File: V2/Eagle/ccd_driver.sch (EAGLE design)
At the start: 103 parts, among them J3 POWER_JACK, Q1 1A/60V/2.4Ω, Q2 BC214, Q3 2N2222, U1 LM358DT, U10 TPD4S012DRYR, U11 0ZCJ0050FF2G, U12 REF3025AIDBZR, U2 MK02FN128VLF10, U5 CP2102N-A01-GQFN20R

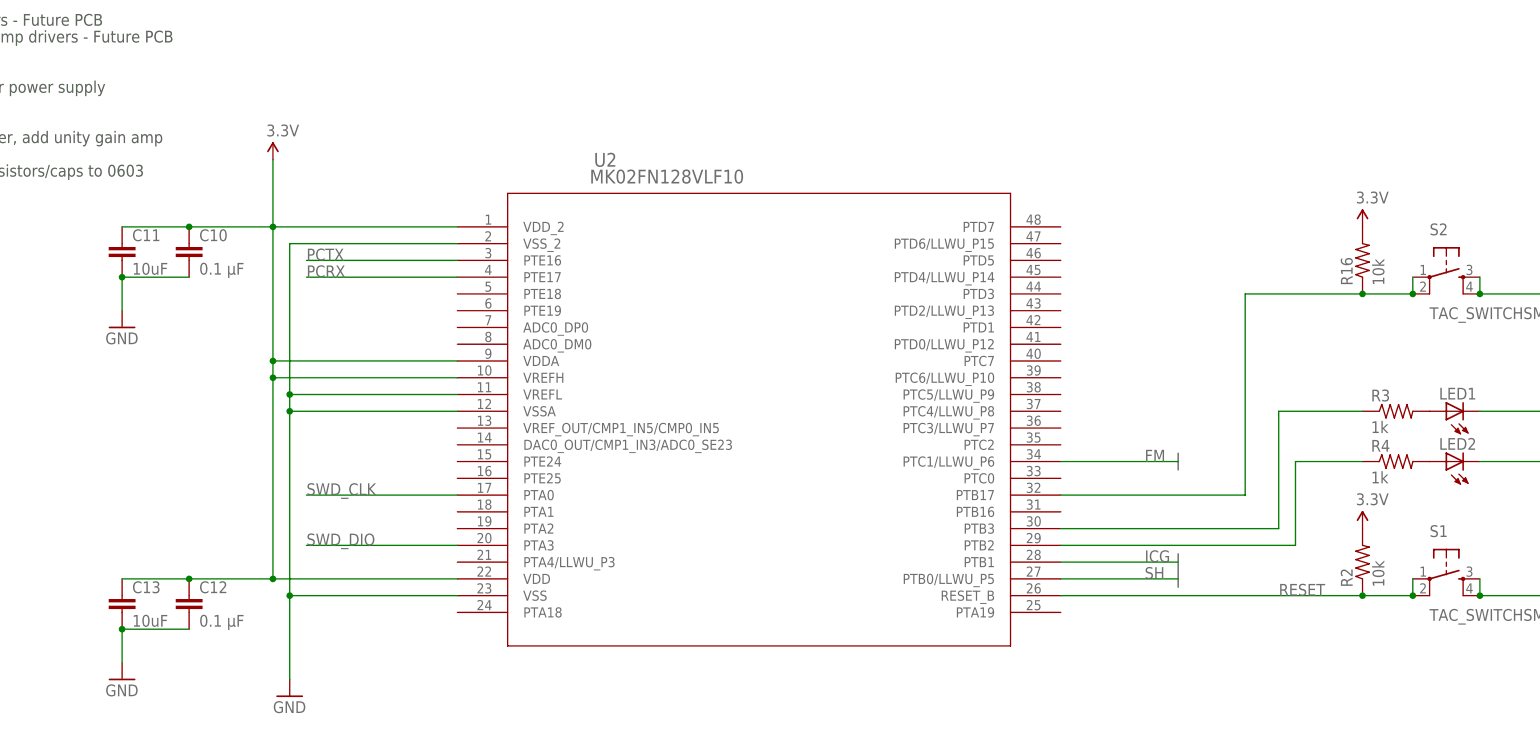
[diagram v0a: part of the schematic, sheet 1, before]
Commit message: changed most caps and resistors to 0603
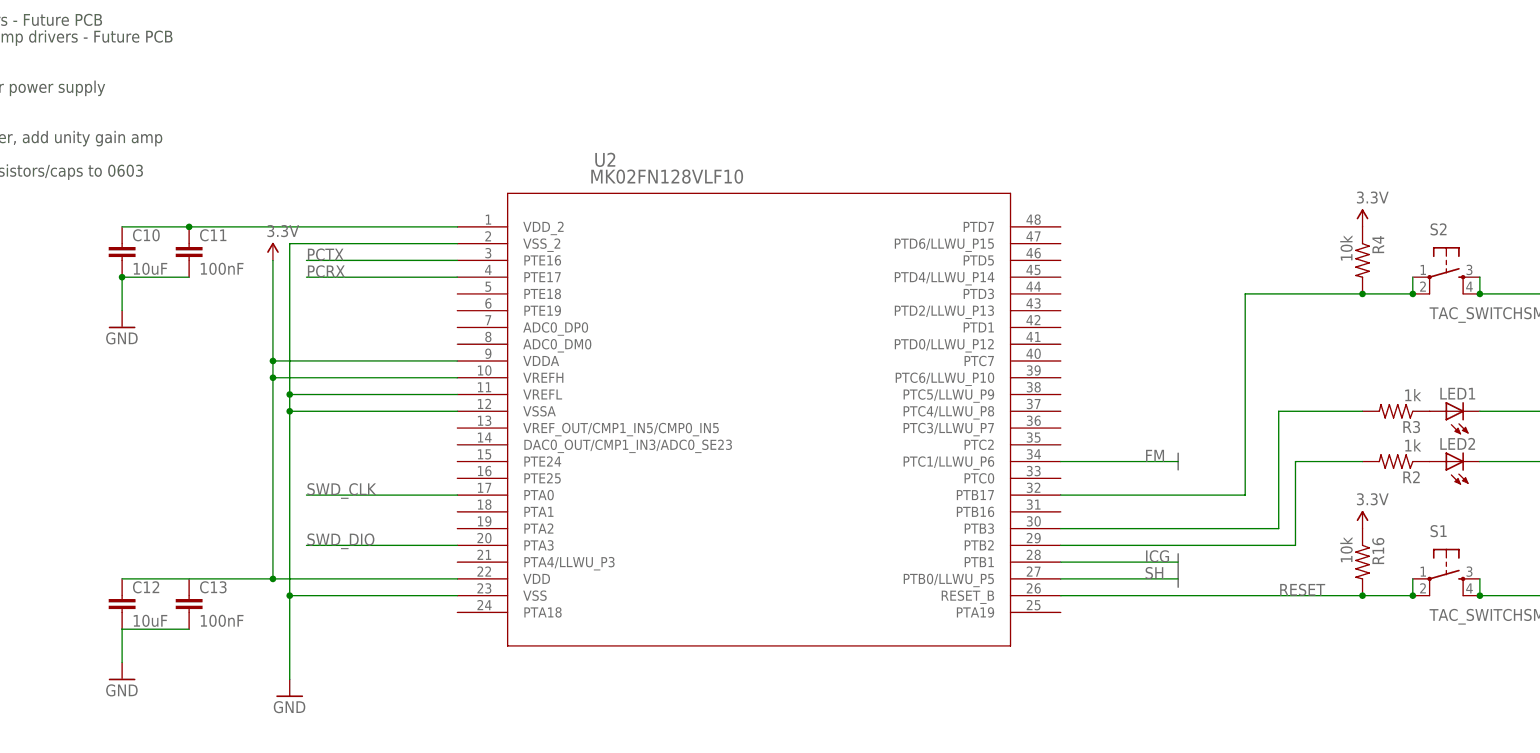
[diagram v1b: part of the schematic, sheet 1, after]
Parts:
- C10, C12: value 0.1 µF -> 10uF; device resistor:C-EUC1206 -> SparkFun-Capacitors:0.1UF-0603-25V-(+80/-20%)
- C11, C13: value 10uF -> 100nF; device resistor:C-EUC1206 -> SparkFun-Capacitors:0.1UF-0603-25V-(+80/-20%)
- C5, C6: device resistor:C-EUC1206 -> SparkFun-Capacitors:10PF-50V-5%(0603)
- R16, R3: device resistor:R-US_R0805 -> audio amplifier example:R-US_R0603
- R2: value 10k -> 1k; device resistor:R-US_R0805 -> audio amplifier example:R-US_R0603
- R4: value 1k -> 10k; device resistor:R-US_R0805 -> audio amplifier example:R-US_R0603
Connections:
- removed net N$13: LED2.A, R4.2
- new net N$37: C10.1, C11.1, U2.VDD_2
- net 3.3V: now also R16.1, R4.1; no longer C10.1, C11.1, C12.1, C13.1, R16.2, R2.2, U2.VDD_2
- net GND: no longer C12.2, C13.2
- net N$11: now also R3.2; no longer R3.1
- net N$12: now also R3.1; no longer R3.2
- net N$15: no longer R4.1
- net N$7: now also R4.2; no longer R16.1
- net RESET: now also R16.2; no longer R2.1
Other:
- moved on the sheet: C10, C11, C12, C13, C5, C6, R16, R2, R3, R4

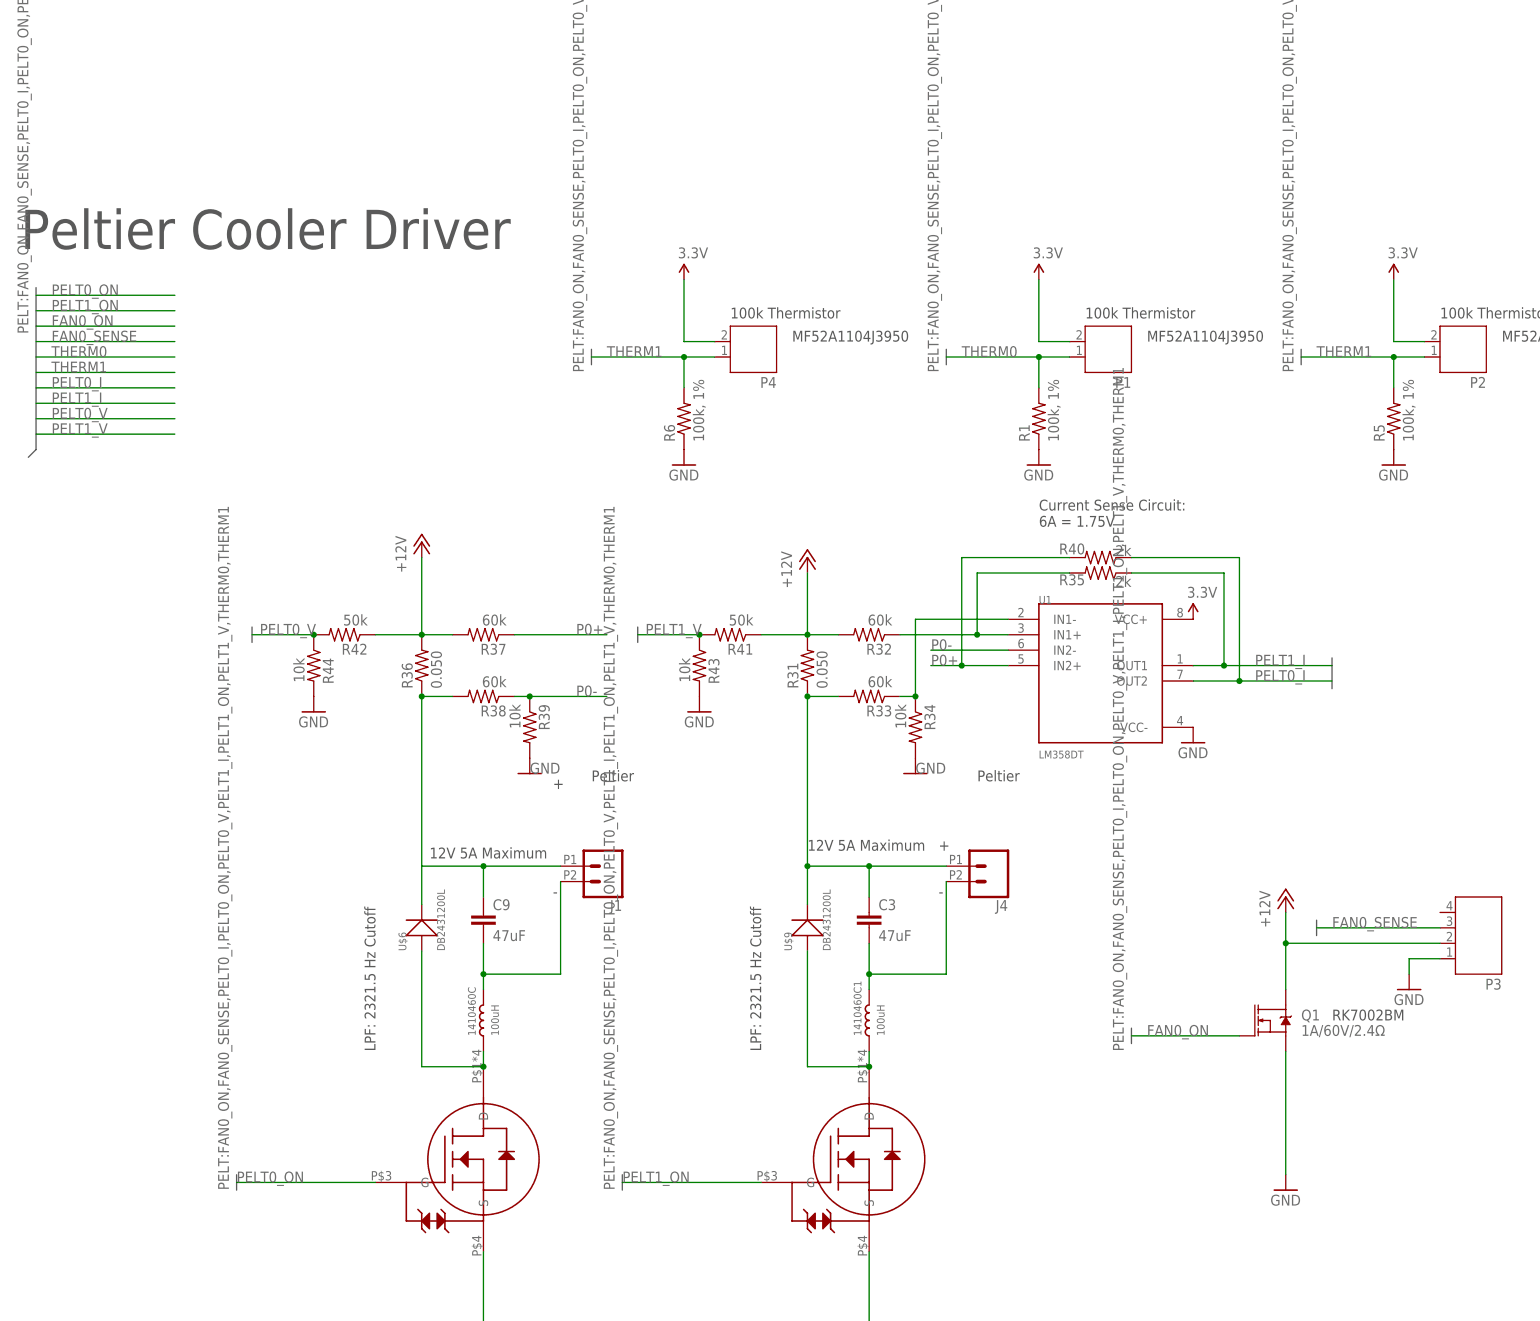
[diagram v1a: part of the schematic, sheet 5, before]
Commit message: fixed fan circuit
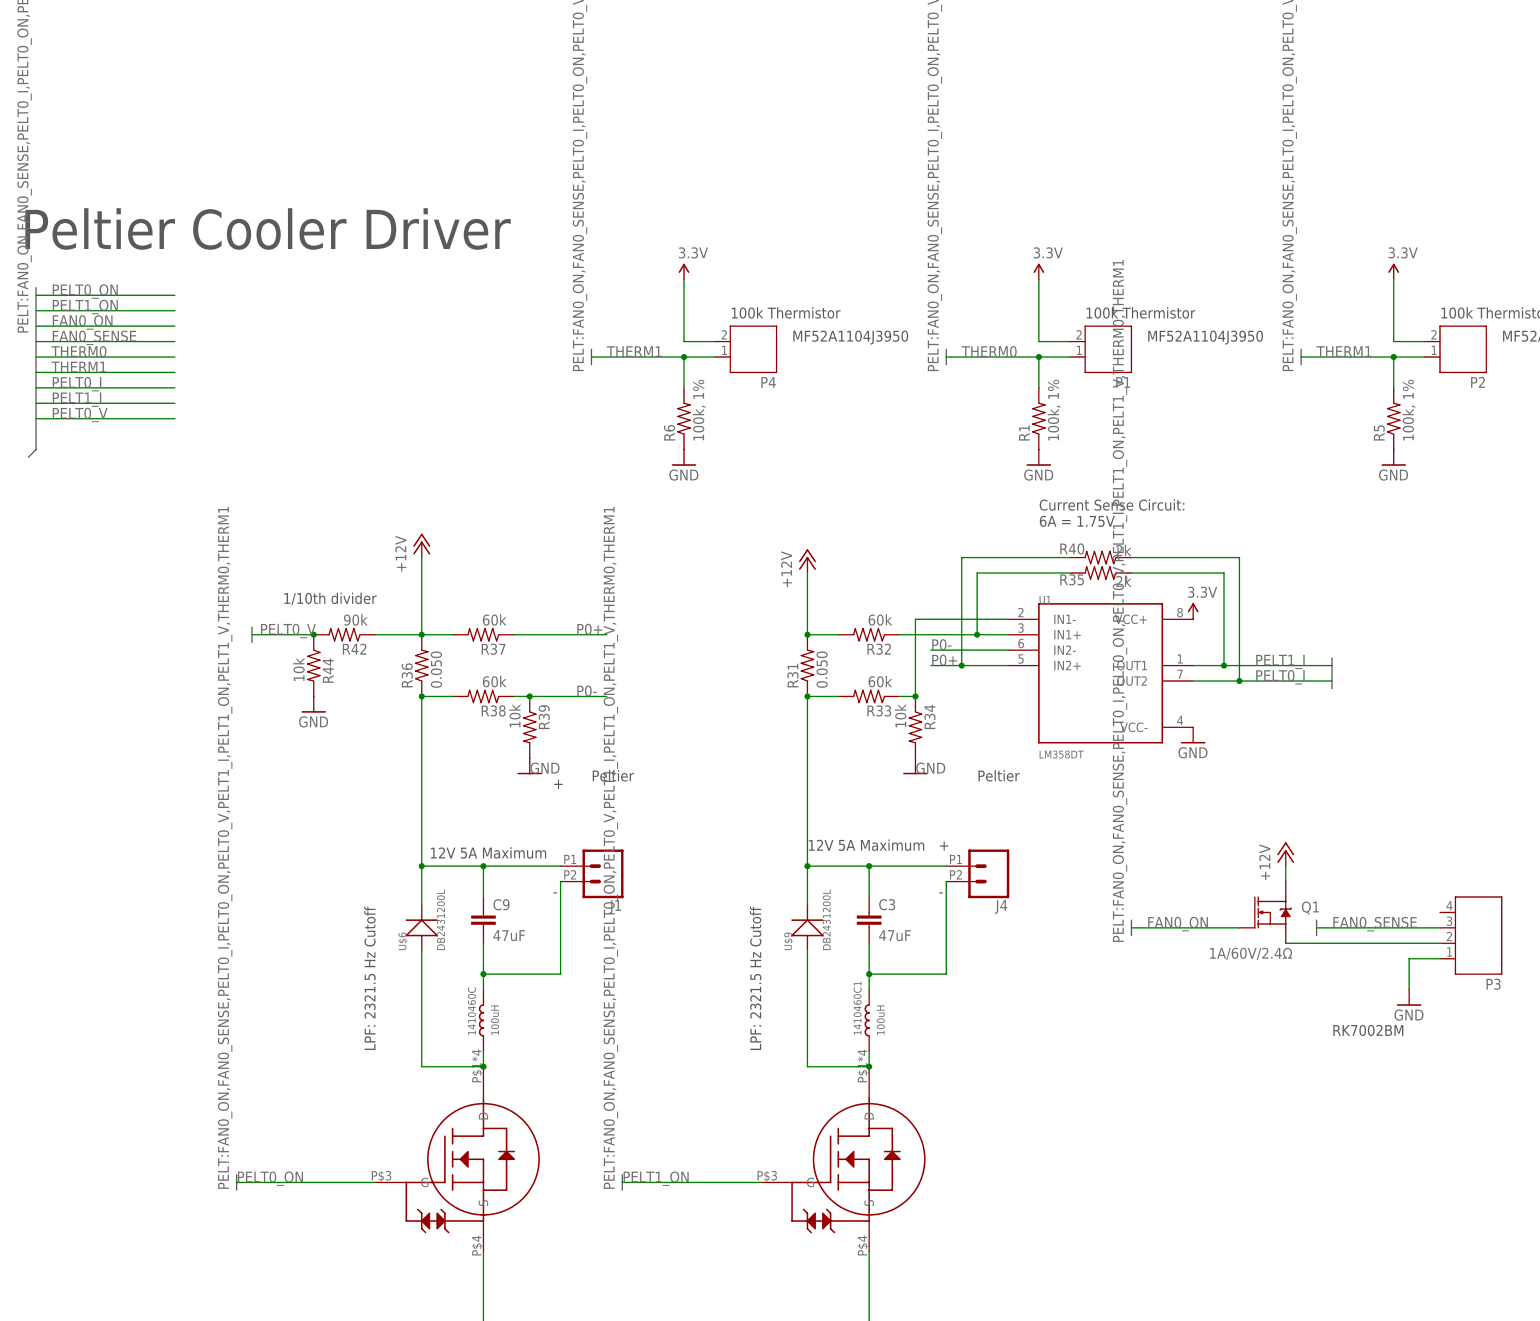
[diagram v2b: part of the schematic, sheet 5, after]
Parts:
- removed R41: 50k, audio amplifier example:R-US_R0603
- removed R43: 10k, audio amplifier example:R-US_R0603
- R42: value 50k -> 90k
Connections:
- removed net N$36: R36.1, R38.2
- removed net PELT1_V: R41.2, R43.1
- new net N$13: P3.2, Q1.S
- net +12V: no longer P3.2, R41.1
- net GND: no longer Q1.S, R43.2
- net N$38: now also R36.1, R38.2
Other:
- note added: "1/10th divider"
- note added: "Precision 3V voltage ref"
- moved on the sheet: C61, C62, Q1, U12

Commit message: removed current sense because its not very smart
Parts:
- removed R31, R36: 0.050, resistor:R-US_R2512
- removed R32, R33, R37, R38: 60k, audio amplifier example:R-US_R0603
- removed R34, R39: 10k, audio amplifier example:R-US_R0603
- removed R35, R40: 2k, audio amplifier example:R-US_R0603
- removed U1: LM358DT, LM358DT:LM358DT
- added R41, R45: 50k, audio amplifier example:R-US_R0603
- added R43, R46, R48: 10k, audio amplifier example:R-US_R0603
- added R47: 60k, audio amplifier example:R-US_R0603
- added R49, R50: 2k, audio amplifier example:R-US_R0603
- added U3: LM358DT, LM358DT:LM358DT
- R42: value 90k -> 0.050; device audio amplifier example:R-US_R0603 -> resistor:R-US_R2512
- R44: value 10k -> 60k
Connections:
- removed net +12V1: R42.1
- removed net N$26: R33.1, R34.1, U1.IN1-
- removed net N$27: R32.1, R35.2, U1.IN1+
- removed net N$38: C9.1, J1.1, R36.1, R38.2, U$6.-
- removed net N$4: C3.1, J4.1, R31.1, R33.2, U$9.-
- new net N$36: R42.1, R47.2
- new net N$39: R47.1, R48.1, U3.IN1-
- new net N$40: R44.1, R49.2, U3.IN1+
- new net PELT1_V: R45.2, R46.1
- net +12V: now also C3.1, C9.1, J1.1, J4.1, R42.2, R44.2, U$6.-, U$9.-; no longer R31.2, R32.2, R36.2, R37.2
- net 3.3V: now also U3.VCC+; no longer U1.VCC+
- net GND: now also R43.2, R46.2, R48.2, U3.VCC-; no longer R34.2, R39.2, R44.2, U1.VCC-
- net N$1: now also R45.1
- net N$16: now also R41.1
- net P0+: now also R50.2, U3.IN2+; no longer R37.1, R40.2, U1.IN2+
- net P0-: now also U3.IN2-; no longer R38.1, R39.1, U1.IN2-
- net PELT0_I: now also R50.1, U3.OUT2; no longer R40.1, U1.OUT2
- net PELT0_V: now also R41.2, R43.1; no longer R42.2, R44.1
- net PELT1_I: now also R49.1, U3.OUT1; no longer R35.1, U1.OUT1
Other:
- moved on the sheet: 1410460C, 1410460C1, C3, C9, J1, J4, P1, P2, P4, R1, R42, R44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

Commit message: overhauled power subsection. Changed LC values for lpfs. Minor changes, added sim for output
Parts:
- removed 1410460C, 1410460C1: 100uH, DMN1019UVT:1410460C
- removed 486R8SC: 6.8 uF, LMR23630:486R8SC
- removed C42: 10uF, SparkFun-Capacitors:10UF-1210-50V-20%
- removed C43: 2.2uF, SparkFun-Capacitors:10PF-50V-5%(0603)
- removed C44: 75 pF, SparkFun-Capacitors:10PF-50V-5%(0603)
- removed C45: 470 nF, SparkFun-Capacitors:10PF-50V-5%(0603)
- removed R42: 0.050, resistor:R-US_R2512
- removed R44, R47: 60k, audio amplifier example:R-US_R0603
- removed R48: 10k, audio amplifier example:R-US_R0603
- removed R49, R50: 2k, audio amplifier example:R-US_R0603
- removed U$6, U$9: DB2431200L, DMN1019UVT:DB2431200L
- removed U$7: LMR23630, LMR23630:LMR23630
- removed U$8: R1966ABLKBLKFR, LMR23630:R1966ABLKBLKFR
- removed U3: LM358DT, LM358DT:LM358DT
- added C110: 10uF, rcl:C-EUC0805
- added C17: 10uF, eagle-ltspice:CC1206
- added C69: 2.2uF, SparkFun-Capacitors:10PF-50V-5%(0603)
- added C70, C92: 47 pF, SparkFun-Capacitors:10PF-50V-5%(0603)
- added C77: 100nF, SparkFun-Capacitors:10PF-50V-5%(0603)
- added C79: UWZ1C151MCL1GS, caps:UWZ1C151MCL1GS
- added C88: 10uF, SparkFun-Capacitors:10PF-50V-5%(0603)
- added C95: 0.47uF, SparkFun-Capacitors:10PF-50V-5%(0603)
- added C99: EMVE160ADA101MF55G, LM2776DBVR:EMVE160ADA101MF55G
- added CR1: SMAJ54CA, fuses:SMAJ54CA
- added D1, D2: DB2431200L, DMN1019UVT:DB2431200L
- added D3: BZX84C12-TP, diode:ZENER-DIODESOT23
- added D4: BZX84C39, diode:ZENER-DIODESOT23
- added F1, F2, F3, F6: 2920PTC, fuses:2920PTC
- added J5: (no value), SparkFun-Connectors:CONN_023.5MM
- added L1, L2: 2.2uF, PhotoSpec_Parts:VLS6045EX
- added L11: 486R8SC, LMR23630:486R8SC
- added L9: CIGW252010GLR47MNE, LM2776DBVR:CIGW252010GLR47MNE
- added LED14: SML-LX23, lightpipes:SML-LX23
- added R31, R53: 1k, audio amplifier example:R-US_R0603
- added R36: 0, audio amplifier example:R-US_R0603
- added R40: 22.1k, audio amplifier example:R-US_R0603
- added R51: 470, audio amplifier example:R-US_R0603
- added R54: 6k, audio amplifier example:R-US_R0603
- added TP9: TPPAD1-13, testpad:TPPAD1-13
- added U13: DMP6023LE-13, fuses:DMP6023LE-13
- added U14: LMR23630, LMR23630:LMR23630
- added U4: ADS7946SRTER, ADS7946:ADS7946SRTER
- added U8: S602TSRP, fuses:BT168GW
- C3, C9: value 47uF -> 470uF; device SparkFun-Capacitors:10UF-1210-50V-20% -> PhotoSpec_Parts:UWT1C471MNL1GS
- R18: value 22.1k -> 51k
- R19: value 51k -> 88.7k
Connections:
- removed net N$33: C45.1, U$7.BOOT
- removed net N$34: 486R8SC.2, C44.1, R19.2
- removed net N$35: J3.PWR, U$8.1
- removed net N$36: R42.1, R47.2
- removed net N$39: R47.1, R48.1, U3.IN1-
- removed net N$40: R44.1, R49.2, U3.IN1+
- removed net P0+: R50.2, U3.IN2+
- removed net P0-: U3.IN2-
- removed net PELT0_I: R50.1, U3.OUT2
- removed net PELT1_I: R49.1, U3.OUT1
- new net +VIN: C110.1, D3.C, D4.C, R54.1, U13.S, U14.VIN, U8.A
- new net N$26: LED2.A, R2.1
- new net N$4: D3.A, R19.2, U13.G
- new net N$61: C69.1, U14.VCC
- new net N$66: R53.1, R54.2, U14.EN/SYNC
- new net N$70: C70.2, C92.2, R18.1, R40.2, U14.FB
- new net N$76: C95.2, L11.1, U14.SW
- new net N$79: C95.1, U14.BOOT
- new net N$88: C70.1, C77.1, C79.11, C88.1, C92.1, L11.2, L9.1, R18.2, R51.1
- new net N$89: F6.P$1, R36.2, TP9.TP
- new net N$91: LED14.A, R51.2
- new net N$95: C99.22, F6.P$2, L9.2
- net +12V: now also F1.P$1, F2.P$1, J5.2; no longer C3.1, C9.1, J1.1, J4.1, R42.2, R44.2, U$6.-, U$9.-
- net 3.3V: now also C12.1, C13.1, R36.1; no longer U3.VCC+
- net GND: now also C110.2, C12.2, C13.2, C17.2, C69.2, C77.2, C79.22, C88.2, C99.11, CR1.1, J5.1, LED14.C, R19.1, R31.1, R40.1, R53.2, U14.AGND, U14.PGND, U8.K; no longer C42.2, C43.2, R48.2, U$7.AGND, U$7.PGND, U3.VCC-
- net N$1: now also C3.22, L2.2; no longer 1410460C1.2, C3.2
- net N$14: now also CR1.2, F3.P$2, J3.PWR; no longer C43.1, U$7.VCC
- net N$15: now also R2.2
- net N$16: now also C9.22, L1.2; no longer 1410460C.2, C9.2
- net N$17: now also D2.+, L1.1; no longer 1410460C.1, U$6.+
- net N$18: now also C9.11, D2.-, F1.P$2, J1.1; no longer 486R8SC.1, C45.2, U$7.SW
- net N$2: now also D1.+, L2.1; no longer 1410460C1.1, U$9.+
- net N$21: now also C3.11, D1.-, F2.P$2, J4.1; no longer C42.1, U$7.EN/SYNC, U$7.VIN, U$8.2
- net N$25: now also F3.P$1, U13.D; no longer C44.2, R18.2, R19.1, U$7.FB
- net N$5: now also C17.1, D4.A, R31.2, U8.G; no longer R18.1
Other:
- note added: "12V high power supply for peltiers only"
- note added: "13kHz LC Filter"
- note added: "5-36V Tolerant Input, 3.3V Out"
- note added: "5kHz LC filter"
- note added: "ESD"
- note added: "Output Ripple ~0.1V"
- note added: "Over Voltage"
- note added: "Reverse Voltage"
- note added: "Switching Frequency = 400kHz"
- note added: "TODO: Add low ripple analog voltage"
- note added: "TODO: Add negative rail"
- note added: "TODO: Add nice power switch"
- note added: "TODO: Add proper power supply [X]"
- note removed: "36V Tolerant Input, 3.3V Out"
- note removed: "Current Sense Circuit: 6A = 1.75V"
- note removed: "Peltier"
- note removed: "TODO: Add proper power supply"
- note removed: "X7R || X5R >=16V"
